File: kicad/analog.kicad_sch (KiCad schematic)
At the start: 23 parts, among them J25 ADC #1 in 0, J26 ADC #1 in 2, J27 ADC #1 in 3, U5 ADS1115IDGSR, U6 TLV9062IDR

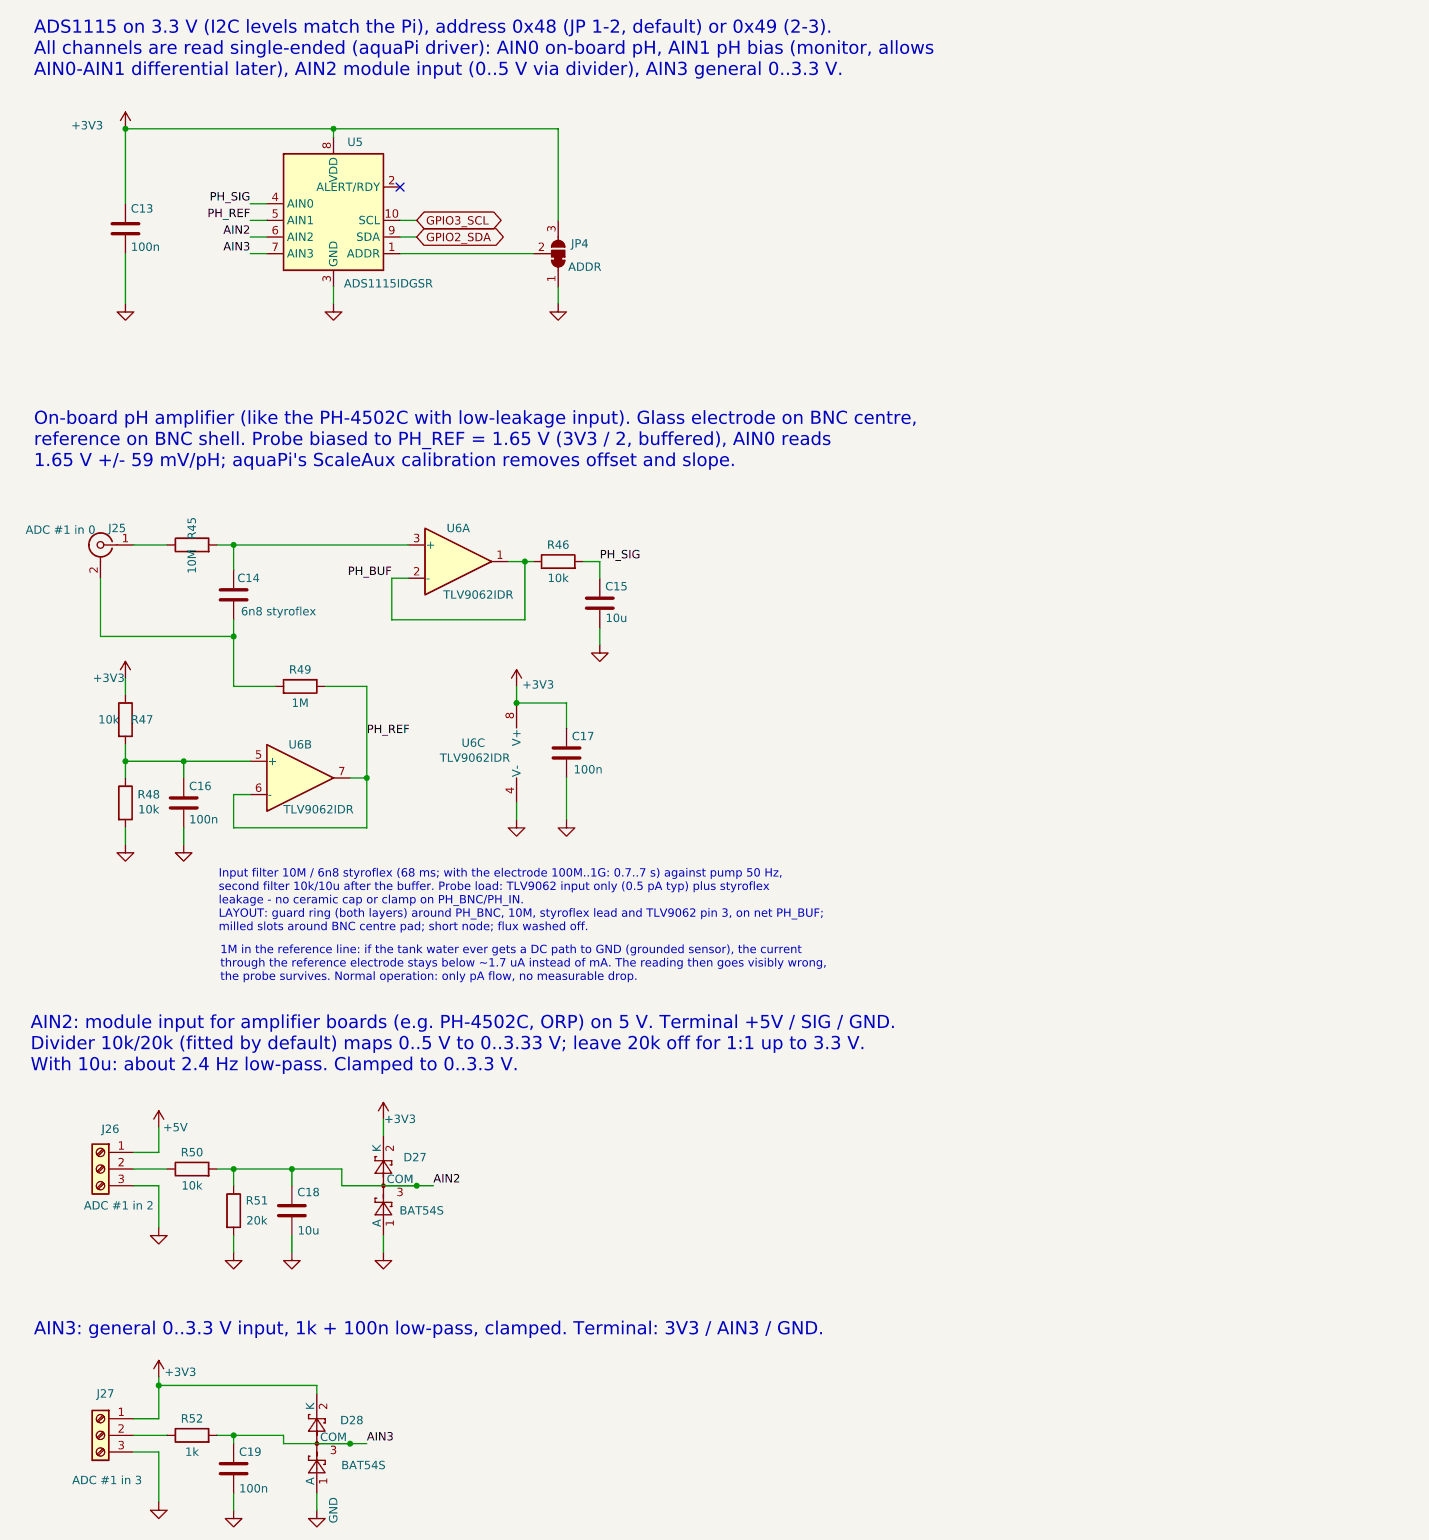
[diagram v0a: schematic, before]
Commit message: kicad: strip obsolete v1 parts for v2 (SSR sheet, IN1..IN4, pH front end)
41 parts, their tracks/vias, pH guard zones, BNC keep-out and port silk removed; freed J2/U5 pins marked no-connect. ERC 0, DRC 0, parity 0; one expected +3V3 ratsnest to J24/JP3/J27/D28 left for the v2 layout.

Co-Authored-By: Claude Opus 5.5 <noreply@anthropic.com>
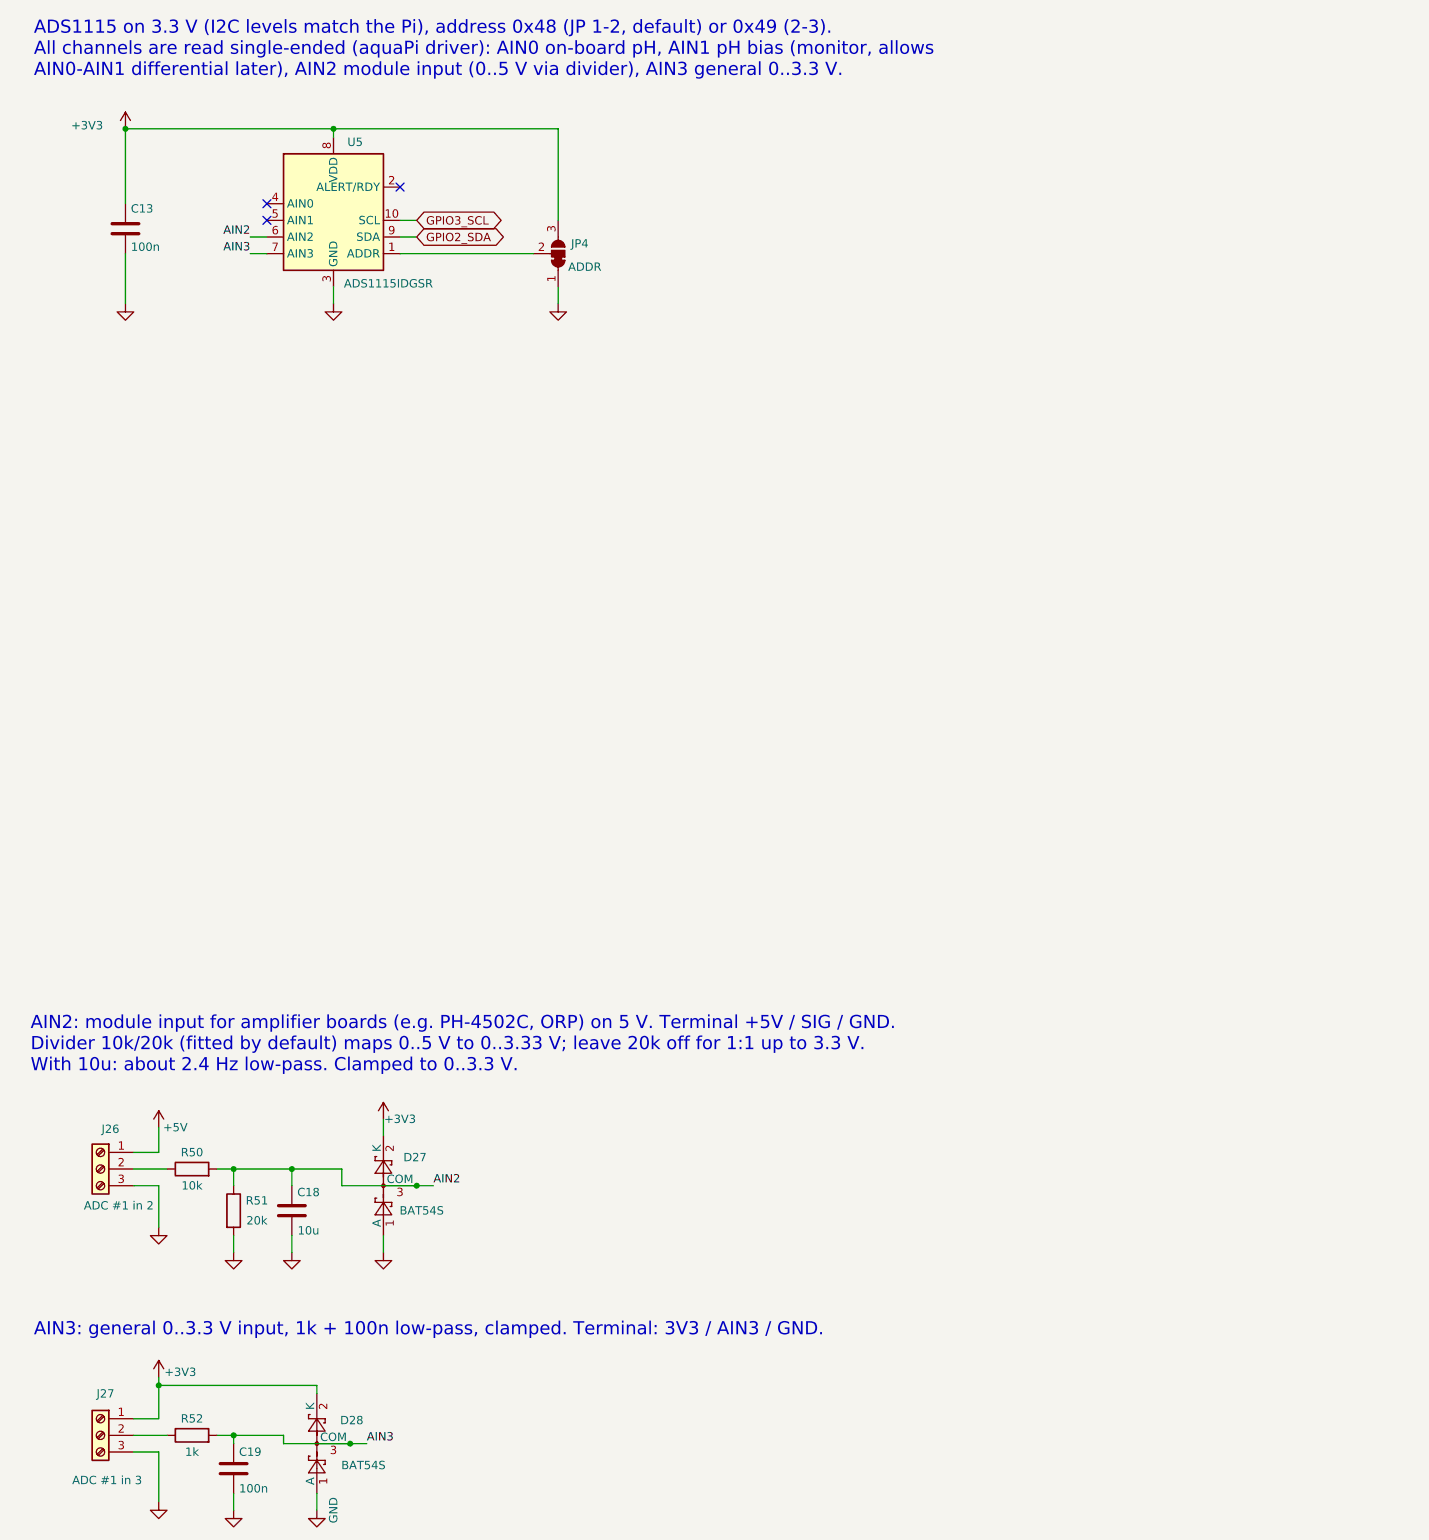
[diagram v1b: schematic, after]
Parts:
- removed C14: 6n8 styroflex, Capacitor_THT:C_Axial_L12.0mm_D6.5mm_P15.00mm_Horizontal, symbol Device:C
- removed C15: 10u, Capacitor_SMD:C_0805_2012Metric, symbol Device:C
- removed C16, C17: 100n, Capacitor_SMD:C_0805_2012Metric, symbol Device:C
- removed J25: ADC #1 in 0, aquaPCB:BNC_HanElectricity_BNC-Q9-50KWE_Horizontal, symbol Connector:Conn_Coaxial
- removed R45: 10M, Resistor_SMD:R_0805_2012Metric, symbol Device:R
- removed R46, R47, R48: 10k, Resistor_SMD:R_0805_2012Metric, symbol Device:R
- removed R49: 1M, Resistor_SMD:R_0805_2012Metric, symbol Device:R
- removed U6: TLV9062IDR, Package_SO:SOIC-8_3.9x4.9mm_P1.27mm, symbol Amplifier_Operational:TLV9062xD
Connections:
- net PH_REF: no longer names the net of U5.5 (AIN1)
- net PH_SIG: no longer names the net of U5.4 (AIN0)
- no-connect marks 1 -> 3
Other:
- note removed: "1M in the reference line: if the tank water ever gets a DC path to GND (grounded sensor), the current through the reference electrode stays below ~1.7 uA instead of mA. The reading then goes visibly wrong, the probe survives. Normal operation: only pA flow, no measurable drop."
- note removed: "Input filter 10M / 6n8 styroflex (68 ms; with the electrode 100M..1G: 0.7..7 s) against pump 50 Hz, second filter 10k/10u after the buffer. Probe load: TLV9062 input only (0.5 pA typ) plus styroflex leakage - no ceramic cap or clamp on PH_BNC/PH_IN. LAYOUT: guard ring (both layers) around PH_BNC, 10M, styroflex lead and TLV9062 pin 3, on net PH_BUF; milled slots around BNC centre pad; short node;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"
- note removed: "On-board pH amplifier (like the PH-4502C with low-leakage input). Glass electrode on BNC centre, reference on BNC shell. Probe biased to PH_REF = 1.65 V (3V3 / 2, buffered), AIN0 reads 1.65 V +/- 59 mV/pH; aquaPi's ScaleAux calibration removes offset and slope."

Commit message: kicad: v2 schematic and board update (PCA9685 x2, box-header ports, sensors, analog sockets)
New sheets pwm/powerbar/sensors; Q2/3/5/6 on PCA #1 ch 15-12; sensor GPIOs 5,6,20,21,22,23; 1-Wire +5V_EXT/Data/GND; four identical 0-5 V analog sockets; DC/LED/sensor ports as 2x4 box headers (pin n = Robo-Tank v3 RJ45 pin n). Board: 82 new footprints coarse-placed (56 parked beside the board), ERC 0, DRC copper 0, parity 0. README v2 plan updated.

Co-Authored-By: Claude Opus 5.5 <noreply@anthropic.com>
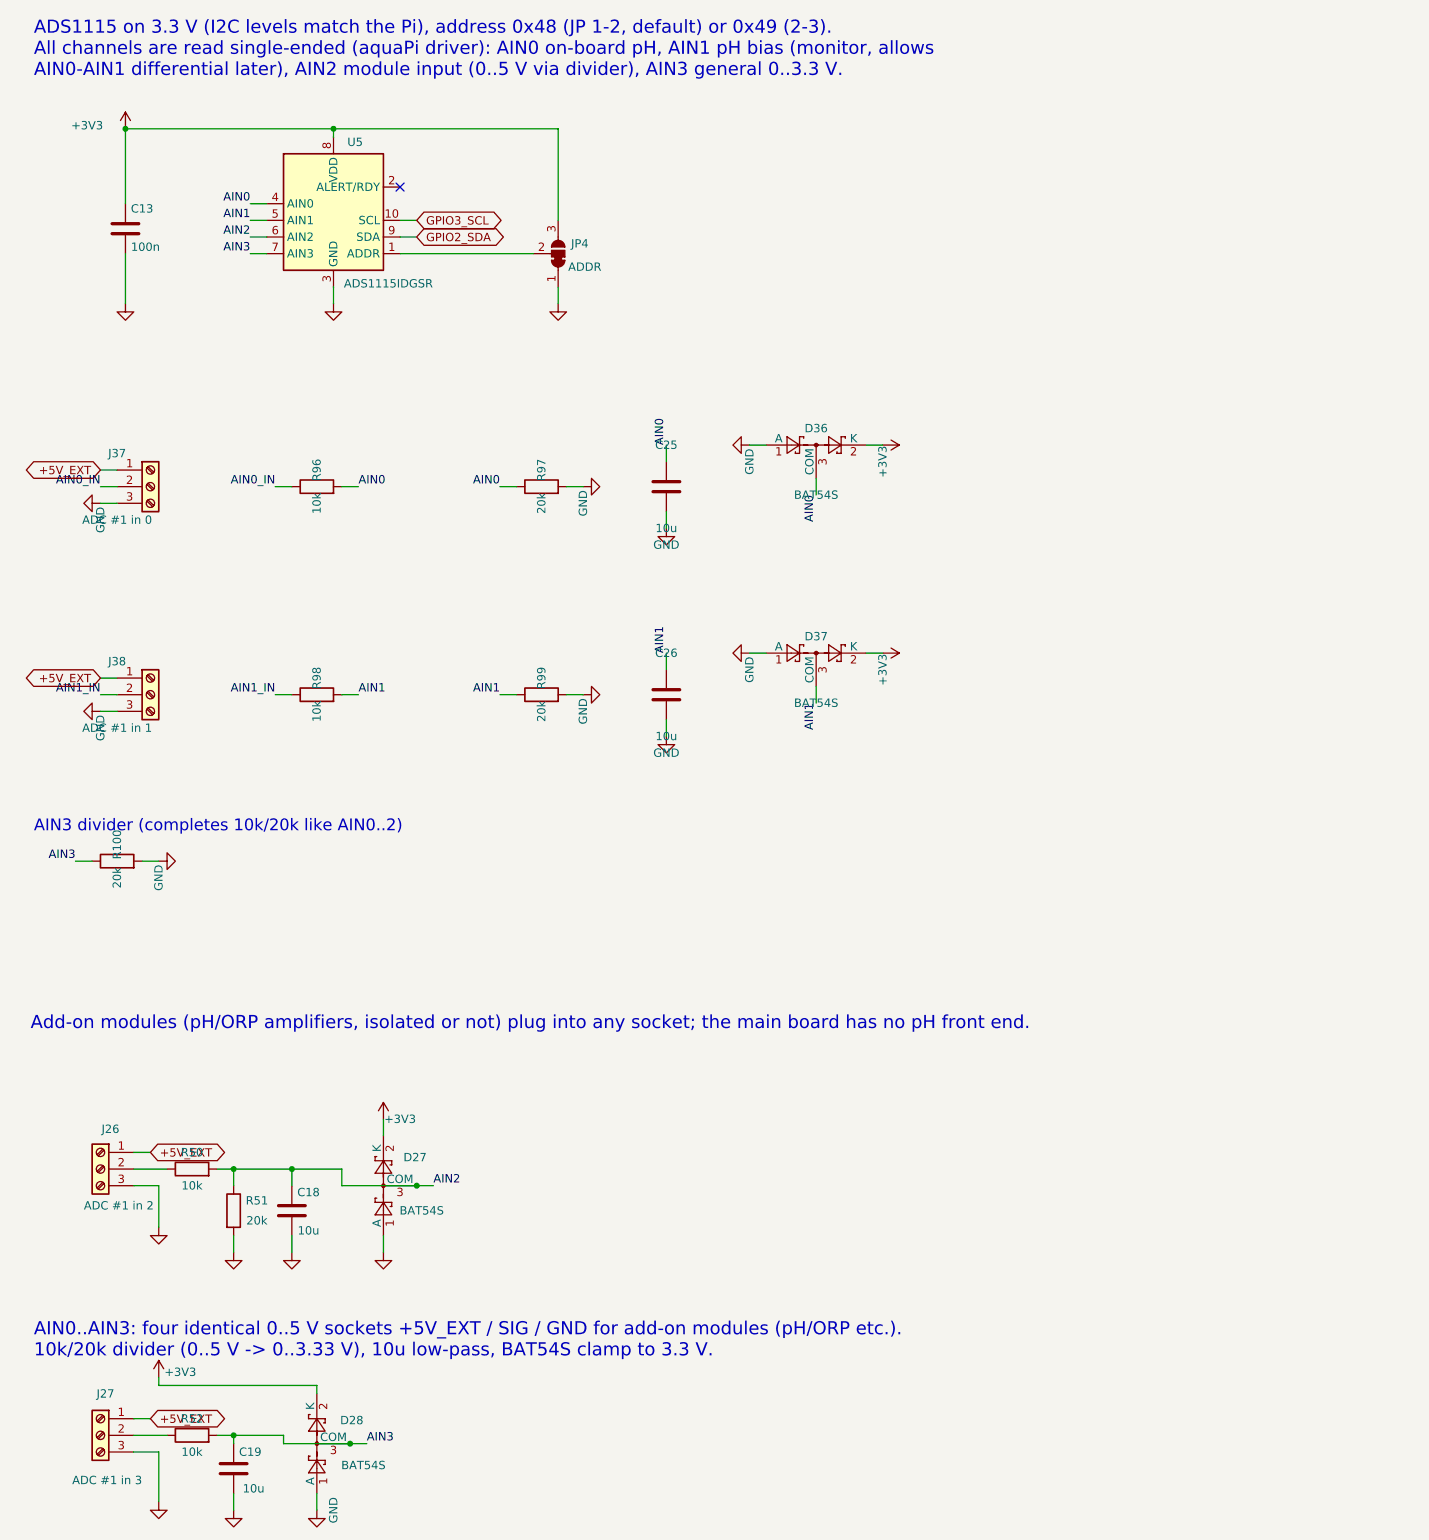
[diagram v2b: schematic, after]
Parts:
- added C25, C26: 10u, Capacitor_SMD:C_0805_2012Metric, symbol Device:C
- added D36, D37: BAT54S, Package_TO_SOT_SMD:SOT-23, symbol Diode:BAT54S
- added J37: ADC #1 in 0, aquaPCB:TerminalBlock_Kangnex_WJ250B-3.5-03P_P3.50mm_Staggered, symbol Connector:Screw_Terminal_01x03
- added J38: ADC #1 in 1, aquaPCB:TerminalBlock_Kangnex_WJ250B-3.5-03P_P3.50mm_Staggered, symbol Connector:Screw_Terminal_01x03
- added R100, R97, R99: 20k, Resistor_SMD:R_0805_2012Metric, symbol Device:R
- added R96, R98: 10k, Resistor_SMD:R_0805_2012Metric, symbol Device:R
- C19: value 100n -> 10u; LCSC C49678 -> C15850
- R52: value 1k -> 10k; LCSC C17513 -> C17414
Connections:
- net +3V3: now also D36.2 (K), D37.2 (K); no longer J27.1 (Pin_1)
- net AIN3: now also R100.1
- net GND: now also C25.2, C26.2, D36.1 (A), D37.1 (A), J37.3 (Pin_3), J38.3 (Pin_3), R100.2, R97.2, R99.2
- net AIN0: now reaches U5.4 (AIN0)
- net AIN0: now also C25.1, D36.3 (COM), R96.2, R97.1
- net AIN1: now reaches U5.5 (AIN1)
- net AIN1: now also C26.1, D37.3 (COM), R98.2, R99.1
- net +5V renamed +5V_EXT
- net +5V_EXT: now also J27.1 (Pin_1), J37.1 (Pin_1), J38.1 (Pin_1)
- new net AIN0_IN: J37.2 (Pin_2), R96.1
- new net AIN1_IN: J38.2 (Pin_2), R98.1
- no-connect marks 3 -> 1
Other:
- note added: "AIN0..AIN3: four identical 0..5 V sockets +5V_EXT / SIG / GND for add-on modules (pH/ORP etc.). 10k/20k divider (0..5 V -> 0..3.33 V), 10u low-pass, BAT54S clamp to 3.3 V."
- note added: "AIN3 divider (completes 10k/20k like AIN0..2)"
- note added: "Add-on modules (pH/ORP amplifiers, isolated or not) plug into any socket; the main board has no pH front end."
- note removed: "AIN2: module input for amplifier boards (e.g. PH-4502C, ORP) on 5 V. Terminal +5V / SIG / GND. Divider 10k/20k (fitted by default) maps 0..5 V to 0..3.33 V; leave 20k off for 1:1 up to 3.3 V. With 10u: about 2.4 Hz low-pass. Clamped to 0..3.3 V."
- note removed: "AIN3: general 0..3.3 V input, 1k + 100n low-pass, clamped. Terminal: 3V3 / AIN3 / GND."
